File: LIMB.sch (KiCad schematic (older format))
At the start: 53 parts, among them J2 MICROSD, J6 DEBUG, M1 FAN-4PIN, Q12 FK3303010L, Q13 FK3303010L, Q20 FK3303010L, Q21 FK3303010L, Q3 IRLML6402, U10 MAX3232PW, U11 NUF2042XV6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

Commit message: Route P3V3_SUSP
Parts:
- added C134, C135, C136, C137, C138, C139, C140, C141: 1u, IPC7351-Nominal:CAPC1005X55, symbol C-0402
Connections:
- net A10 is gone; now on net ~CARDEN: LIMB1.54 (PC28)
- net A13 is gone; now on net BRIDGE_SUSP: LIMB1.8 (PC31)
- net A17 is gone; now on net USB_VBSENSE: LIMB1.74 (PA0)
- net BRIDGE_SUSP: no longer LIMB1.14 (PA18)
- net GND: now also C134.2, C135.2, C136.2, C137.2, C138.2, C139.2, C140.2, C141.2
- net P3V3_STBY: now also C134.1, C136.1, C138.1, C140.1
- net VCORE: now reaches LIMB1.100 (VPLL), LIMB1.11 (VDDOUT), LIMB1.16 (VCORE), LIMB1.36 (VCORE), LIMB1.56 (VCORE), LIMB1.85 (VCORE)
- net VCORE: now also C135.1, C137.1, C139.1, C141.1
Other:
- moved on the sheet: C130, C131, C9, J2, J6, LIMB1, M1, Q3, R102, R103, R104, R116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

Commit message: Add voltage sense for several rails
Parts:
- added R139, R140, R141, R143, R144: 5k1, IPC7351-Nominal:RESC1005X40, symbol R-0402
- added R142: 51k, IPC7351-Nominal:RESC1005X40, symbol R-0402
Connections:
- net GND: now also R141.1, R143.1
- net P12V_PCI: now also R142.2
- net P3V3_STBY: now also R139.2
- net SENSE3V3: now reaches LIMB1.12 (PA17)
- net SENSE3V3: now also R139.1, R141.2
- net SENSE1V2: now reaches LIMB1.14 (PA18)
- net SENSE1V2: now also R140.1
- net A11 renamed SENSE12V
- net SENSE12V: now also R142.1, R143.2
- net A12 renamed SENSE1V5
- net SENSE1V5: now also R144.1
- new net P1V2_CORE: R140.2
- new net P1V5_BRIDGE: R144.2

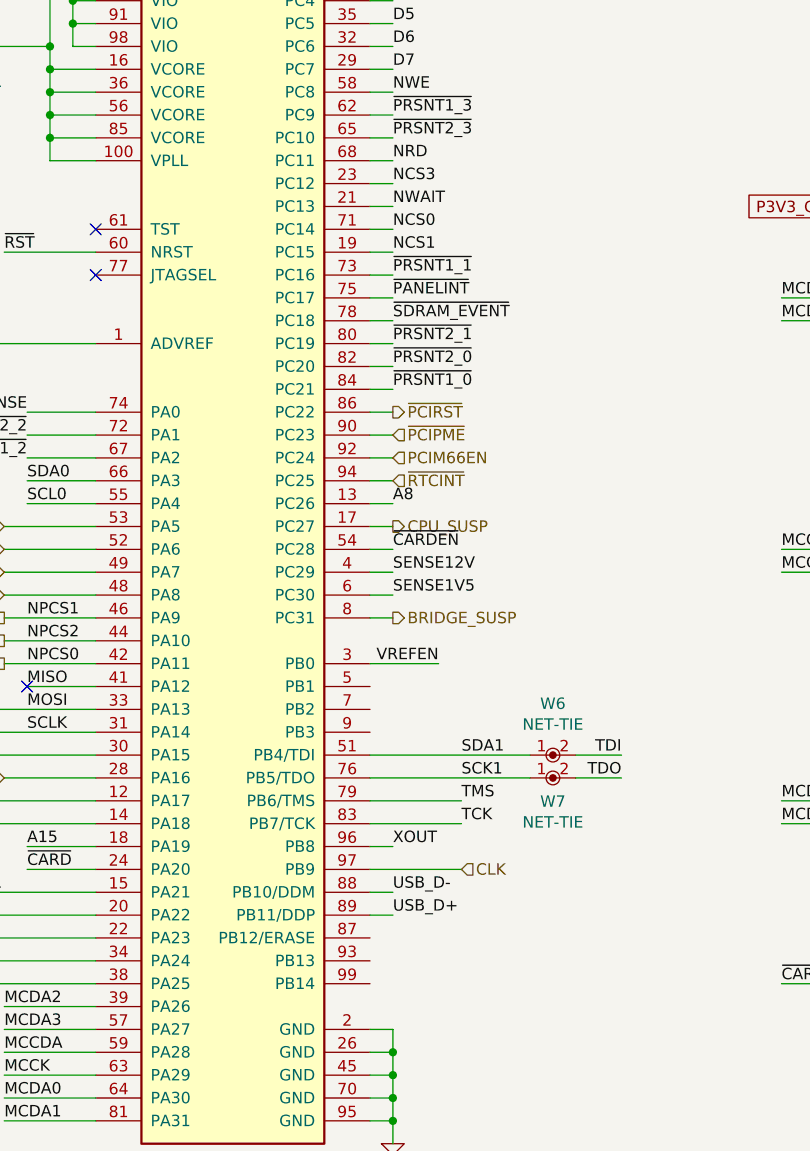
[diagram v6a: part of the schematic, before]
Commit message: Run ERC and connect missing D6
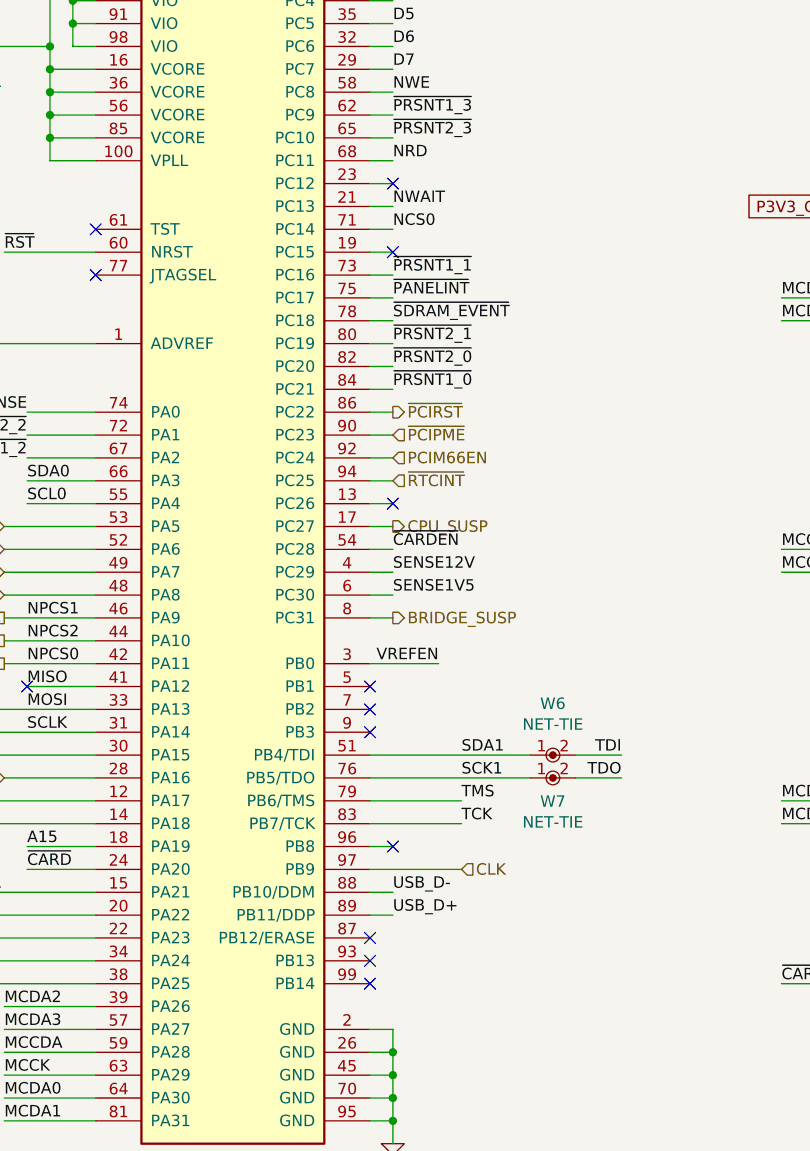
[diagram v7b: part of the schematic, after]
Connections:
- net A8: no longer names the net of LIMB1.13 (PC26)
- net NCS1: no longer names the net of LIMB1.19 (PC15)
- net NCS3: no longer names the net of LIMB1.23 (PC12)
- net XOUT: no longer names the net of LIMB1.96 (PB8)
- no-connect marks 4 -> 14
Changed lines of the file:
@@
 	1    0    0    -1
 $EndComp
-Text Label 4400 3900 0    50   ~ 0
-A8
 Text Label 2800 5400 0    50   ~ 0
 A15
@@
 Text Label 4400 2700 0    50   ~ 0
 NCS0
-Text Label 4400 2800 0    50   ~ 0
-NCS1
-Text Label 4400 2500 0    50   ~ 0
-NCS3
 Text Label 4400 2400 0    50   ~ 0
 NRD
@@
 Text Label 4400 5600 0    50   ~ 0
 USB_D-
-Text Label 4400 5400 0    50   ~ 0
-XOUT
-$Comp
-L GND #PWR224
+$Comp
+L GND #PWR0236
 U 1 1 577EAB82
 P 4400 6700
-F 0 "#PWR224" H 4400 6700 30  0001 C CNN
+F 0 "#PWR0236" H 4400 6700 30  0001 C CNN
 F 1 "GND" H 4400 6630 30  0001 C CNN
 F 2 "" H 4400 6700 60  0000 C CNN
@@
 $EndComp
 $Comp
-L GND #PWR234
+L GND #PWR0237
 U 1 1 577EDCE7
 P 10400 4700
-F 0 "#PWR234" H 10400 4700 30  0001 C CNN
+F 0 "#PWR0237" H 10400 4700 30  0001 C CNN
 F 1 "GND" H 10400 4630 30  0001 C CNN
 F 2 "" H 10400 4700 60  0000 C CNN
@@
 MCDA3
 $Comp
-L GND #PWR233
+L GND #PWR0238
 U 1 1 577EDF0A
 P 10400 4000
-F 0 "#PWR233" H 10400 4000 30  0001 C CNN
+F 0 "#PWR0238" H 10400 4000 30  0001 C CNN
 F 1 "GND" H 10400 3930 30  0001 C CNN
 F 2 "" H 10400 4000 60  0000 C CNN
@@
 P3V3_CARD
 $Comp
-L GND #PWR231
+L GND #PWR0239
 U 1 1 577EEC84
 P 9600 4200
-F 0 "#PWR231" H 9600 4200 30  0001 C CNN
+F 0 "#PWR0239" H 9600 4200 30  0001 C CNN
 F 1 "GND" H 9600 4130 30  0001 C CNN
 F 2 "" H 9600 4200 60  0000 C CNN
@@
 ~RST
 $Comp
-L GND #PWR223
+L GND #PWR0240
 U 1 1 579F6A32
 P 2800 8000
-F 0 "#PWR223" H 2800 8000 30  0001 C CNN
+F 0 "#PWR0240" H 2800 8000 30  0001 C CNN
 F 1 "GND" H 2800 7930 30  0001 C CNN
 F 2 "" H 2800 8000 60  0000 C CNN
@@
 $EndComp
 $Comp
-L GND #PWR243
+L GND #PWR0241
 U 1 1 57A172F2
 P 14750 1650
-F 0 "#PWR243" H 14750 1650 30  0001 C CNN
+F 0 "#PWR0241" H 14750 1650 30  0001 C CNN
 F 1 "GND" H 14750 1580 30  0001 C CNN
 F 2 "" H 14750 1650 60  0000 C CNN
@@
 $EndComp
 $Comp
-L GND #PWR239
+L GND #PWR0242
 U 1 1 57A1D8E5
 P 13950 3400
-F 0 "#PWR239" H 13950 3400 30  0001 C CNN
+F 0 "#PWR0242" H 13950 3400 30  0001 C CNN
 F 1 "GND" H 13950 3330 30  0001 C CNN
 F 2 "" H 13950 3400 60  0000 C CNN
@@
 $EndComp
 $Comp
-L GND #PWR237
+L GND #PWR0243
 U 1 1 57A1DE24
 P 12050 3400
-F 0 "#PWR237" H 12050 3400 30  0001 C CNN
+F 0 "#PWR0243" H 12050 3400 30  0001 C CNN
 F 1 "GND" H 12050 3330 30  0001 C CNN
 F 2 "" H 12050 3400 60  0000 C CNN
@@
 $EndComp
 $Comp
-L GND #PWR236
+L GND #PWR0244
 U 1 1 57A1E179
 P 11800 3250
-F 0 "#PWR236" H 11800 3250 30  0001 C CNN
+F 0 "#PWR0244" H 11800 3250 30  0001 C CNN
 F 1 "GND" H 11800 3180 30  0001 C CNN
 F 2 "" H 11800 3250 60  0000 C CNN
@@
 P3V3_STBY
 $Comp
-L GND #PWR238
+L GND #PWR0245
 U 1 1 57A1EEA9
 P 12300 4200
-F 0 "#PWR238" H 12300 4200 30  0001 C CNN
+F 0 "#PWR0245" H 12300 4200 30  0001 C CNN
 F 1 "GND" H 12300 4130 30  0001 C CNN
 F 2 "" H 12300 4200 60  0000 C CNN
@@
 $EndComp
 $Comp
-L GND #PWR245
+L GND #PWR0246
 U 1 1 57A22C9D
 P 14900 4450
-F 0 "#PWR245" H 14900 4450 30  0001 C CNN
+F 0 "#PWR0246" H 14900 4450 30  0001 C CNN
 F 1 "GND" H 14900 4380 30  0001 C CNN
 F 2 "" H 14900 4450 60  0000 C CNN
@@
 $EndComp
 $Comp
-L GND #PWR242
+L GND #PWR0247
 U 1 1 57A22E58
 P 14600 4450
-F 0 "#PWR242" H 14600 4450 30  0001 C CNN
+F 0 "#PWR0247" H 14600 4450 30  0001 C CNN
 F 1 "GND" H 14600 4380 30  0001 C CNN
 F 2 "" H 14600 4450 60  0000 C CNN
@@
 $EndComp
 $Comp
-L GND #PWR241
+L GND #PWR0248
 U 1 1 57A22FB0
 P 14300 4450
-F 0 "#PWR241" H 14300 4450 30  0001 C CNN
+F 0 "#PWR0248" H 14300 4450 30  0001 C CNN
 F 1 "GND" H 14300 4380 30  0001 C CNN
 F 2 "" H 14300 4450 60  0000 C CNN
@@
 $EndComp
 $Comp
-L GND #PWR240
+L GND #PWR0249
 U 1 1 57A23109
 P 14000 4450
-F 0 "#PWR240" H 14000 4450 30  0001 C CNN
+F 0 "#PWR0249" H 14000 4450 30  0001 C CNN
 F 1 "GND" H 14000 4380 30  0001 C CNN
 F 2 "" H 14000 4450 60  0000 C CNN
@@
 $EndComp
 $Comp
-L GND #PWR232
+L GND #PWR0250
 U 1 1 57A3FEDE
 P 10000 2100
-F 0 "#PWR232" H 10000 2100 30  0001 C CNN
+F 0 "#PWR0250" H 10000 2100 30  0001 C CNN
 F 1 "GND" H 10000 2030 30  0001 C CNN
 F 2 "" H 10000 2100 60  0000 C CNN
@@
 $EndComp
 $Comp
-L GND #PWR230
+L GND #PWR0251
 U 1 1 57A41BDC
 P 9200 2400
-F 0 "#PWR230" H 9200 2400 30  0001 C CNN
+F 0 "#PWR0251" H 9200 2400 30  0001 C CNN
 F 1 "GND" H 9200 2330 30  0001 C CNN
 F 2 "" H 9200 2400 60  0000 C CNN
@@
 $EndComp
 $Comp
-L GND #PWR235
+L GND #PWR0252
 U 1 1 57A49C3C
 P 10500 1750
-F 0 "#PWR235" H 10500 1750 30  0001 C CNN
+F 0 "#PWR0252" H 10500 1750 30  0001 C CNN
 F 1 "GND" H 10500 1680 30  0001 C CNN
 F 2 "" H 10500 1750 60  0000 C CNN
@@
 XUSB_D+
 $Comp
-L GND #PWR244
+L GND #PWR0253
 U 1 1 57AA14DB
 P 14800 2400
-F 0 "#PWR244" H 14800 2400 30  0001 C CNN
+F 0 "#PWR0253" H 14800 2400 30  0001 C CNN
 F 1 "GND" H 14800 2330 30  0001 C CNN
 F 2 "" H 14800 2400 60  0000 C CNN
@@
 Connection ~ 6500 2600
 $Comp
-L GND #PWR227
+L GND #PWR0254
 U 1 1 57A9C7D3
 P 8800 3550
-F 0 "#PWR227" H 8800 3550 30  0001 C CNN
+F 0 "#PWR0254" H 8800 3550 30  0001 C CNN
 F 1 "GND" H 8800 3480 30  0001 C CNN
 F 2 "" H 8800 3550 60  0000 C CNN
@@
 	8800 3500 8700 3500
 $Comp
-L GND #PWR228
+L GND #PWR0255
 U 1 1 57A9C9F3
 P 8800 4650
-F 0 "#PWR228" H 8800 4650 30  0001 C CNN
+F 0 "#PWR0255" H 8800 4650 30  0001 C CNN
 F 1 "GND" H 8800 4580 30  0001 C CNN
 F 2 "" H 8800 4650 60  0000 C CNN
@@
 	8800 4600 8700 4600
 $Comp
-L GND #PWR229
+L GND #PWR0256
 U 1 1 57A9CC0D
 P 8800 5750
-F 0 "#PWR229" H 8800 5750 30  0001 C CNN
+F 0 "#PWR0256" H 8800 5750 30  0001 C CNN
 F 1 "GND" H 8800 5680 30  0001 C CNN
 F 2 "" H 8800 5750 60  0000 C CNN
@@
 Connection ~ 1550 3200
 $Comp
-L GND #PWR215
+L GND #PWR0257
 U 1 1 57AAC080
 P 1550 3700
-F 0 "#PWR215" H 1550 3700 30  0001 C CNN
+F 0 "#PWR0257" H 1550 3700 30  0001 C CNN
 F 1 "GND" H 1550 3630 30  0001 C CNN
 F 2 "" H 1550 3700 60  0000 C CNN
@@
 Connection ~ 1800 3200
 $Comp
-L GND #PWR218
+L GND #PWR0258
 U 1 1 57AB076E
 P 1800 3700
-F 0 "#PWR218" H 1800 3700 30  0001 C CNN
+F 0 "#PWR0258" H 1800 3700 30  0001 C CNN
 F 1 "GND" H 1800 3630 30  0001 C CNN
 F 2 "" H 1800 3700 60  0000 C CNN
@@
 Connection ~ 2400 1900
 $Comp
-L GND #PWR214
+L GND #PWR0259
 U 1 1 57AFC6F6
 P 1200 2300
-F 0 "#PWR214" H 1200 2300 30  0001 C CNN
+F 0 "#PWR0259" H 1200 2300 30  0001 C CNN
 F 1 "GND" H 1200 2230 30  0001 C CNN
 F 2 "" H 1200 2300 60  0000 C CNN
@@
 	1200 2300 1200 2200
 $Comp
-L GND #PWR217
+L GND #PWR0260
 U 1 1 57AFC985
 P 1600 2300
-F 0 "#PWR217" H 1600 2300 30  0001 C CNN
+F 0 "#PWR0260" H 1600 2300 30  0001 C CNN
 F 1 "GND" H 1600 2230 30  0001 C CNN
 F 2 "" H 1600 2300 60  0000 C CNN
@@
 	1600 2300 1600 2200
 $Comp
-L GND #PWR220
+L GND #PWR0261
 U 1 1 57AFCC0E
 P 2000 2300
-F 0 "#PWR220" H 2000 2300 30  0001 C CNN
+F 0 "#PWR0261" H 2000 2300 30  0001 C CNN
 F 1 "GND" H 2000 2230 30  0001 C CNN
 F 2 "" H 2000 2300 60  0000 C CNN
@@
 	2000 2300 2000 2200
 $Comp
-L GND #PWR222
+L GND #PWR0262
 U 1 1 57AFCE98
 P 2400 2300
-F 0 "#PWR222" H 2400 2300 30  0001 C CNN
+F 0 "#PWR0262" H 2400 2300 30  0001 C CNN
 F 1 "GND" H 2400 2230 30  0001 C CNN
 F 2 "" H 2400 2300 60  0000 C CNN
@@
 $EndComp
 $Comp
-L GND #PWR221
+L GND #PWR0263
 U 1 1 57AFD588
 P 2400 1700
-F 0 "#PWR221" H 2400 1700 30  0001 C CNN
+F 0 "#PWR0263" H 2400 1700 30  0001 C CNN
 F 1 "GND" H 2400 1630 30  0001 C CNN
 F 2 "" H 2400 1700 60  0000 C CNN
@@
 $EndComp
 $Comp
-L GND #PWR219
+L GND #PWR0264
 U 1 1 57AFD64A
 P 2000 1700
-F 0 "#PWR219" H 2000 1700 30  0001 C CNN
+F 0 "#PWR0264" H 2000 1700 30  0001 C CNN
 F 1 "GND" H 2000 1630 30  0001 C CNN
 F 2 "" H 2000 1700 60  0000 C CNN
@@
 $EndComp
 $Comp
-L GND #PWR216
+L GND #PWR0265
 U 1 1 57AFD70C
 P 1600 1700
-F 0 "#PWR216" H 1600 1700 30  0001 C CNN
+F 0 "#PWR0265" H 1600 1700 30  0001 C CNN
 F 1 "GND" H 1600 1630 30  0001 C CNN
 F 2 "" H 1600 1700 60  0000 C CNN
@@
 $EndComp
 $Comp
-L GND #PWR213
+L GND #PWR0266
 U 1 1 57AFD7CE
 P 1200 1700
-F 0 "#PWR213" H 1200 1700 30  0001 C CNN
+F 0 "#PWR0266" H 1200 1700 30  0001 C CNN
 F 1 "GND" H 1200 1630 30  0001 C CNN
 F 2 "" H 1200 1700 60  0000 C CNN
@@
 Connection ~ 6100 7300
 $Comp
-L GND #PWR225
+L GND #PWR0267
 U 1 1 57AD7374
 P 6100 7650
-F 0 "#PWR225" H 6100 7650 30  0001 C CNN
+F 0 "#PWR0267" H 6100 7650 30  0001 C CNN
 F 1 "GND" H 6100 7580 30  0001 C CNN
 F 2 "" H 6100 7650 60  0000 C CNN
@@
 Connection ~ 6100 8100
 $Comp
-L GND #PWR226
+L GND #PWR0268
 U 1 1 57ADB7CD
 P 6100 8500
-F 0 "#PWR226" H 6100 8500 30  0001 C CNN
+F 0 "#PWR0268" H 6100 8500 30  0001 C CNN
 F 1 "GND" H 6100 8430 30  0001 C CNN
 F 2 "" H 6100 8500 60  0000 C CNN
@@
 Text Label 4400 4300 0    50   ~ 0
 SENSE1V5
+NoConn ~ 4400 2500
+NoConn ~ 4400 2800
+NoConn ~ 4400 3900
+NoConn ~ 4300 4700
+NoConn ~ 4300 4800
+NoConn ~ 4300 4900
+NoConn ~ 4400 5400
+NoConn ~ 4300 5800
+NoConn ~ 4300 5900
+NoConn ~ 4300 6000
 $EndSCHEMATC
